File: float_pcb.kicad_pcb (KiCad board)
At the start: 2 copper layers, 60 x 60 mm, 62 parts, among them J1 Switch, J2 Conn_01x04, J3 USB_C, J4 Conn_01x03, J5 I2C, J6 Light, J7 Batt, J9 I2C, Q1 AO3400A, Q2 AO3400A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

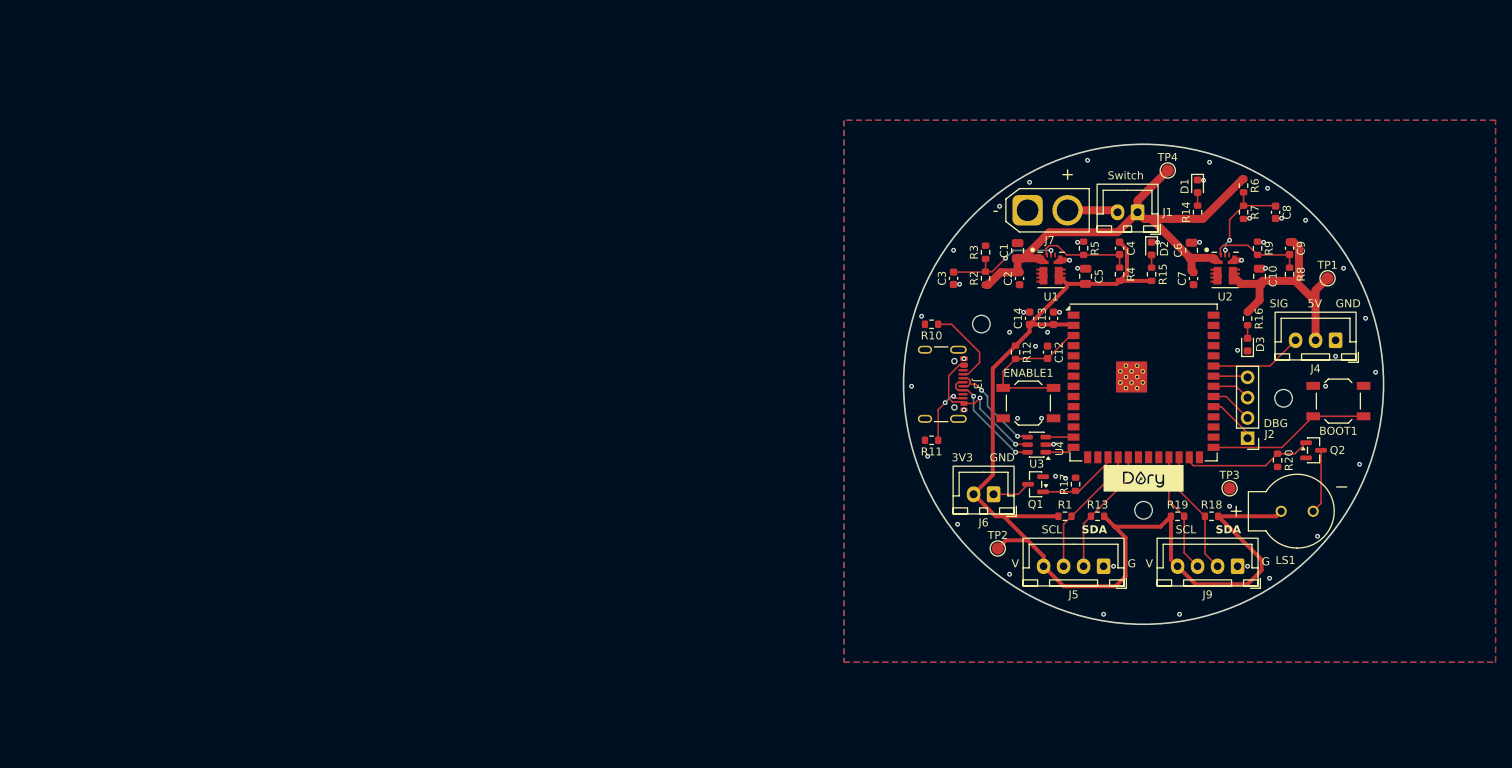
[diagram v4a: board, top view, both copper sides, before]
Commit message: Start of the great multilayer migration
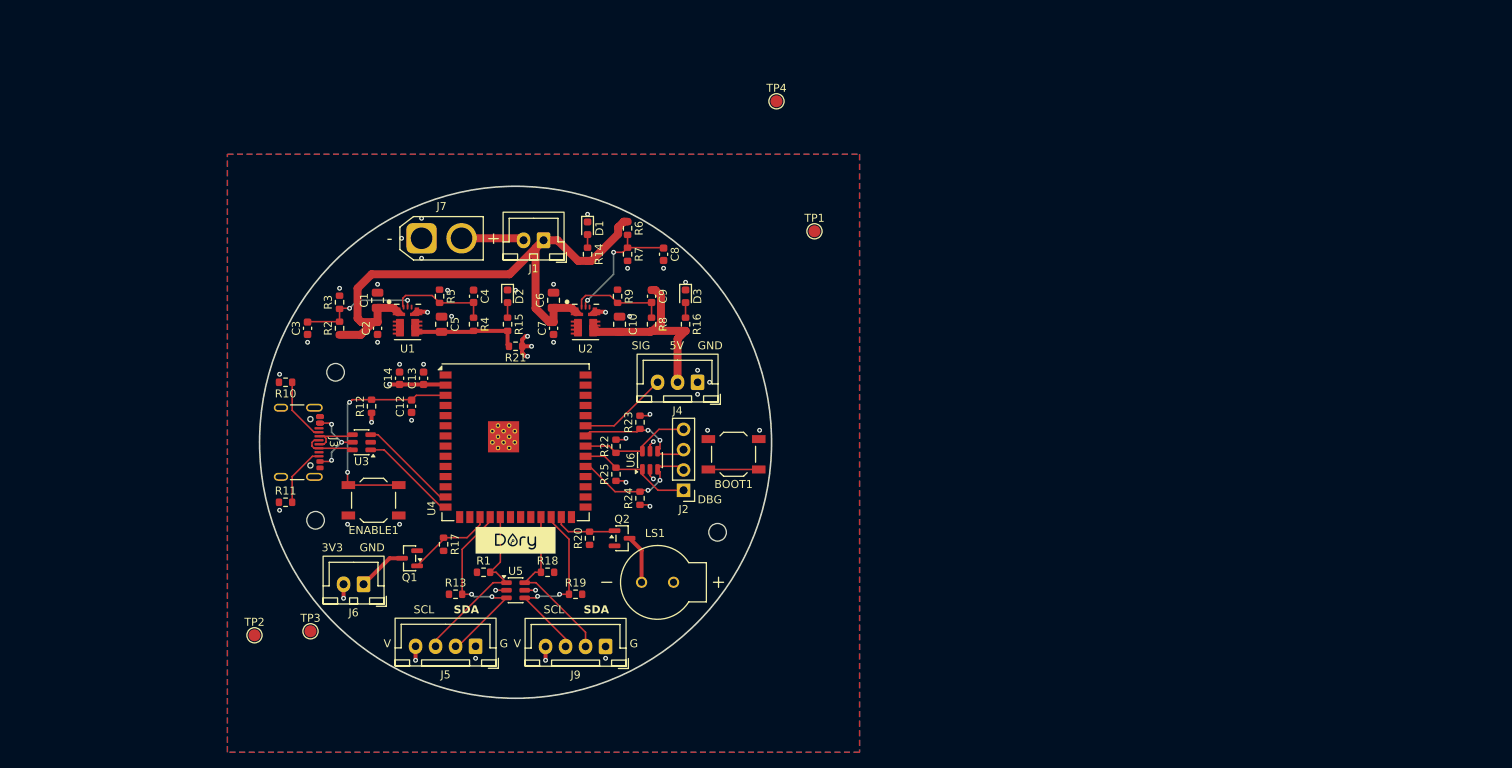
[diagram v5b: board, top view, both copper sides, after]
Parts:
- removed the G*** at (227.3, 102.1)
- added R21: 0, Resistor_SMD:R_0603_1608Metric, F.Cu at (148.5, 93.0)
- added R22: 10k, Resistor_SMD:R_0603_1608Metric, F.Cu at (161.1, 105.5)
- added R23: 10k, Resistor_SMD:R_0603_1608Metric, F.Cu at (164.1, 102.5)
- added R24: 10k, Resistor_SMD:R_0603_1608Metric, F.Cu at (164.1, 112.0)
- added R25: 10k, Resistor_SMD:R_0603_1608Metric, F.Cu at (161.1, 109.0)
- added U5: USBLC6-4SC6, Package_TO_SOT_SMD:SOT-23-6, F.Cu at (148.5, 123.5)
- added U6: USBLC6-4SC6, Package_TO_SOT_SMD:SOT-23-6, F.Cu at (165.3, 107.2)
- moved TP3 116.3 mm to (122.9, 128.6)
- moved H1 102.5 mm to (126.0, 96.2), turned to 0 degrees
- moved TP2 93.5 mm to (115.9, 129.1)
- moved Q2 87.1 mm to (161.8, 117.0)
- moved H3 86.8 mm to (123.5, 114.8)
- moved R20 86.6 mm to (157.8, 117.0), turned to 90 degrees
- moved U3 84.4 mm to (129.2, 105.0)
- moved R18 83.3 mm to (152.5, 121.2)
- moved ENABLE1 82.7 mm to (130.8, 112.2), turned to 180 degrees
- moved R11 81.1 mm to (119.8, 112.5), turned to 0 degrees
- moved R10 81.1 mm to (119.8, 97.5)
- moved C3 81.0 mm to (122.5, 90.8)
- moved R2 81.0 mm to (126.5, 90.8)
- moved R3 81.0 mm to (126.5, 87.5)
- moved R4 81.0 mm to (143.2, 90.2)
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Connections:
- C4 pad 1: +3V3 -> Net-(U1-VOUT)
- C5 pad 2: +3V3 -> Net-(U1-VOUT)
- ENABLE1 pad 1: Net-(U4-EN) -> GND
- ENABLE1 pad 2: GND -> Net-(U4-EN)
- J2 pad 1: Net-(J2-Pin_1) -> MISC1
- J2 pad 2: Net-(J2-Pin_2) -> MISC2
- J2 pad 3: Net-(J2-Pin_3) -> MISC3
- J2 pad 4: Net-(J2-Pin_4) -> MISC4
- R11 pad 1: Net-(J3-CC2) -> GND
- R11 pad 2: GND -> Net-(J3-CC2)
- R13 pad 1: SDA1 -> +3V3
- R13 pad 2: +3V3 -> SDA1
- R14 pad 1: +BATT -> Net-(D1-A)
- R14 pad 2: Net-(D1-A) -> +BATT
- R15 pad 2: +3V3 -> Net-(U1-VOUT)
- R16 pad 1: Net-(J4-Pin_2) -> Net-(D3-A)
- R16 pad 2: Net-(D3-A) -> Net-(J4-Pin_2)
- R19 pad 1: +3V3 -> SCL2
- R19 pad 2: SCL2 -> +3V3
- R20 pad 1: BUZZER -> GND
- R20 pad 2: GND -> BUZZER
- R4 pad 2: +3V3 -> Net-(U1-VOUT)
- TP2 pad 1: +3V3 -> Net-(U1-VOUT)
- U1 pad 3: +3V3 -> Net-(U1-VOUT)
- U4 pad 18: SCL1 -> SDA1
- U4 pad 19: SDA1 -> SCL1
- U4 pad 23: SCL2 -> SDA2
- U4 pad 24: SDA2 -> SCL2
- U4 pad 31: Net-(J2-Pin_1) -> MISC2
- U4 pad 32: Net-(J2-Pin_2) -> MISC1
- U4 pad 33: Net-(J2-Pin_3) -> MISC4
- U4 pad 34: Net-(J2-Pin_4) -> MISC3
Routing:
- net +3V3: track 142.9 -> 26.0 mm, vias 0 -> 14
- net MISC2: track 0.00 -> 16.3 mm, vias 0 -> 2
- net MISC3: track 0.00 -> 15.4 mm, vias 0 -> 2
- net MISC1: track 0.00 -> 14.4 mm
- net MISC4: track 0.00 -> 14.2 mm
- net Net-(U4-IO0): track 20.4 -> 6.30 mm
- net Net-(U1-VOUT): track 0.00 -> 13.8 mm
- net +BATT: track 61.7 -> 72.6 mm
- net Net-(U4-EN): track 19.0 -> 29.2 mm, vias 0 -> 2
- net SDA1: track 15.9 -> 25.7 mm, vias 0 -> 2
- net SCL2: track 15.1 -> 24.5 mm, vias 0 -> 2
- net Net-(U4-USB_D-): track 3.48 -> 12.6 mm
- net /VBUS: track 18.9 -> 9.92 mm, vias 2 -> 3
- net Net-(U4-USB_D+): track 3.73 -> 12.3 mm
- net BUZZER: track 16.5 -> 8.02 mm
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- added copper zone on In2.Cu, net +3V3
- added copper zone on In1.Cu, net GND
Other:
- board size 60 x 60 mm -> 64 x 64 mm
- copper layers 2 -> 4
- board text removed: "NCSSM Morganton Evan Kim '27"
- board text removed: "Switch"
